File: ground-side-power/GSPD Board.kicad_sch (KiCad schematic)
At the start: 34 parts, among them J1 Battery Terminals, J2 Battery Terminals, J3 Battery Terminals, J4 Battery Terminals, J5 Battery Terminals, K1 AZ2150-1A-12DEF, SW1 23A, SW2 SW_SP3T, U1 K7805-3AR3, U2 URB2424LD-20WR3

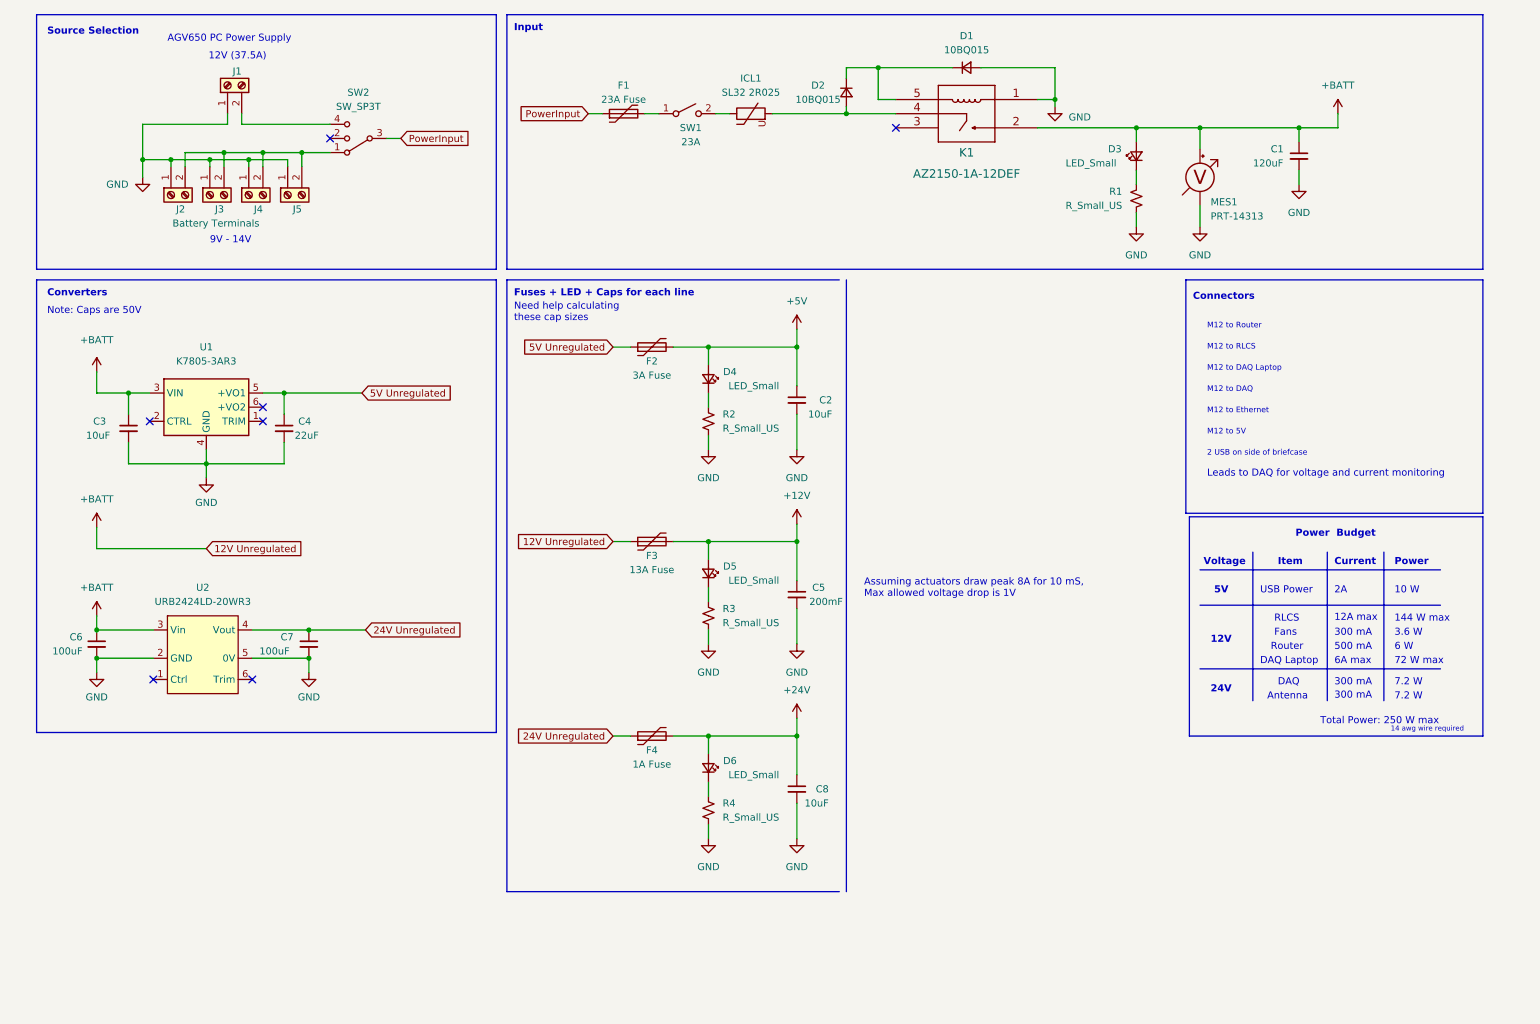
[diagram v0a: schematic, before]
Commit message: Added Screw Terminals for M12 connectors and switches
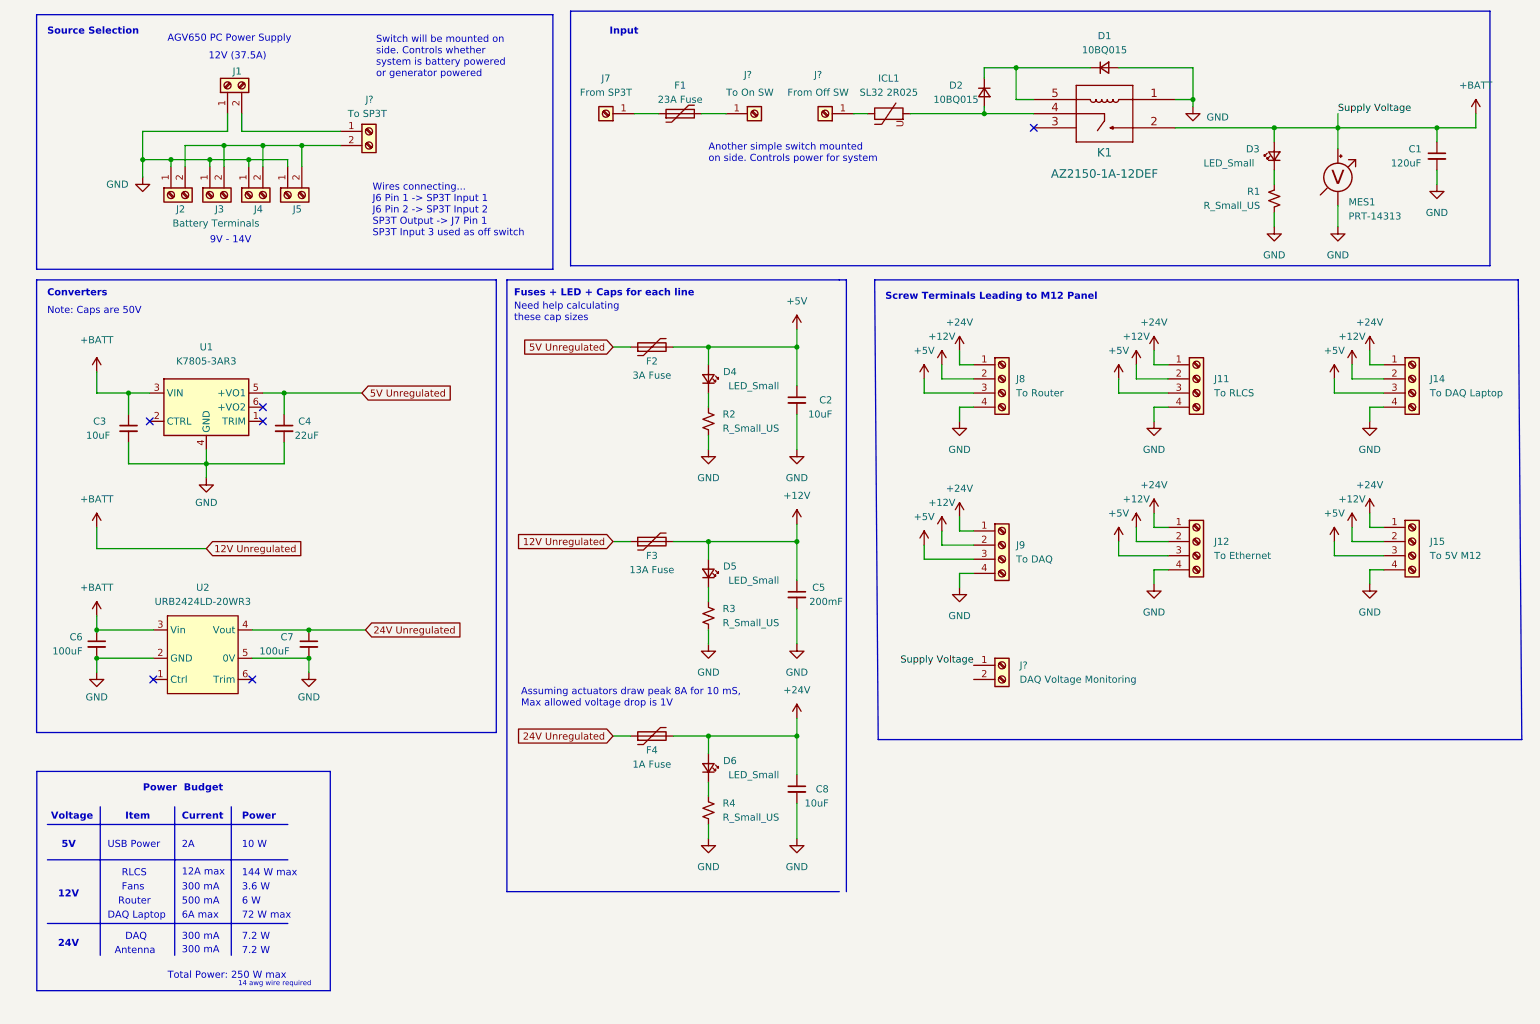
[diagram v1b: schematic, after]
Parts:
- removed SW1: 23A, symbol Switch:SW_SPST
- removed SW2: SW_SP3T, symbol Switch:SW_SP3T
- added J11: To RLCS, symbol Connector:Screw_Terminal_01x04
- added J12: To Ethernet, symbol Connector:Screw_Terminal_01x04
- added J14: To DAQ Laptop, symbol Connector:Screw_Terminal_01x04
- added J15: To 5V M12, symbol Connector:Screw_Terminal_01x04
- added J7: From SP3T, symbol Connector:Screw_Terminal_01x01
- added J8: To Router, symbol Connector:Screw_Terminal_01x04
- added J9: To DAQ, symbol Connector:Screw_Terminal_01x04
- added J?: To On SW, symbol Connector:Screw_Terminal_01x01
- added J?: From Off SW, symbol Connector:Screw_Terminal_01x01
- added J?: DAQ Voltage Monitoring, symbol Connector:Screw_Terminal_01x02
- added J?: To SP3T, symbol Connector:Screw_Terminal_01x02
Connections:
- net +12V: now also J11.2 (Pin_2), J12.2 (Pin_2), J14.2 (Pin_2), J15.2 (Pin_2), J8.2 (Pin_2), J9.2 (Pin_2)
- net +24V: now also J11.1 (Pin_1), J12.1 (Pin_1), J14.1 (Pin_1), J15.1 (Pin_1), J8.1 (Pin_1), J9.1 (Pin_1)
- net +5V: now also J11.3 (Pin_3), J12.3 (Pin_3), J14.3 (Pin_3), J15.3 (Pin_3), J8.3 (Pin_3), J9.3 (Pin_3)
- net +BATT: now also J?.1 (Pin_1)
- net GND: now also J11.4 (Pin_4), J12.4 (Pin_4), J14.4 (Pin_4), J15.4 (Pin_4), J8.4 (Pin_4), J9.4 (Pin_4)
- net at J2.2 (Pin_2), J3.2 (Pin_2), J4.2 (Pin_2)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: now also J?.2 (Pin_2)
- net at J1.2 (Pin_2): now also J?.1 (Pin_1)
- net at ICL1.1: now also J?.1 (Pin_1)
- net at F1.2: now also J?.1 (Pin_1)
- net PowerInput: no longer names the net of F1.1
- net PowerInput: now also J7.1 (Pin_1)
- no-connect marks 7 -> 6
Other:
- note added: "Another simple switch mounted on side. Controls power for system"
- note added: "Screw Terminals Leading to M12 Panel"
- note added: "Switch will be mounted on side. Controls whether system is battery powered or generator powered"
- note added: "Wires connecting... J6 Pin 1 -> SP3T Input 1 J6 Pin 2 -> SP3T Input 2 SP3T Output -> J7 Pin 1 SP3T Input 3 used as off switch"
- note removed: "2 USB on side of briefcase"
- note removed: "Connectors"
- note removed: "Leads to DAQ for voltage and current monitoring"
- note removed: "M12 to 5V"
- note removed: "M12 to DAQ"
- note removed: "M12 to DAQ Laptop"
- note removed: "M12 to Ethernet"
- note removed: "M12 to RLCS"
- note removed: "M12 to Router"
- moved on the sheet: C1, D1, D2, D3, F1, ICL1, K1, MES1, R1

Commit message: Added Current and Voltage Sensing for DAQ
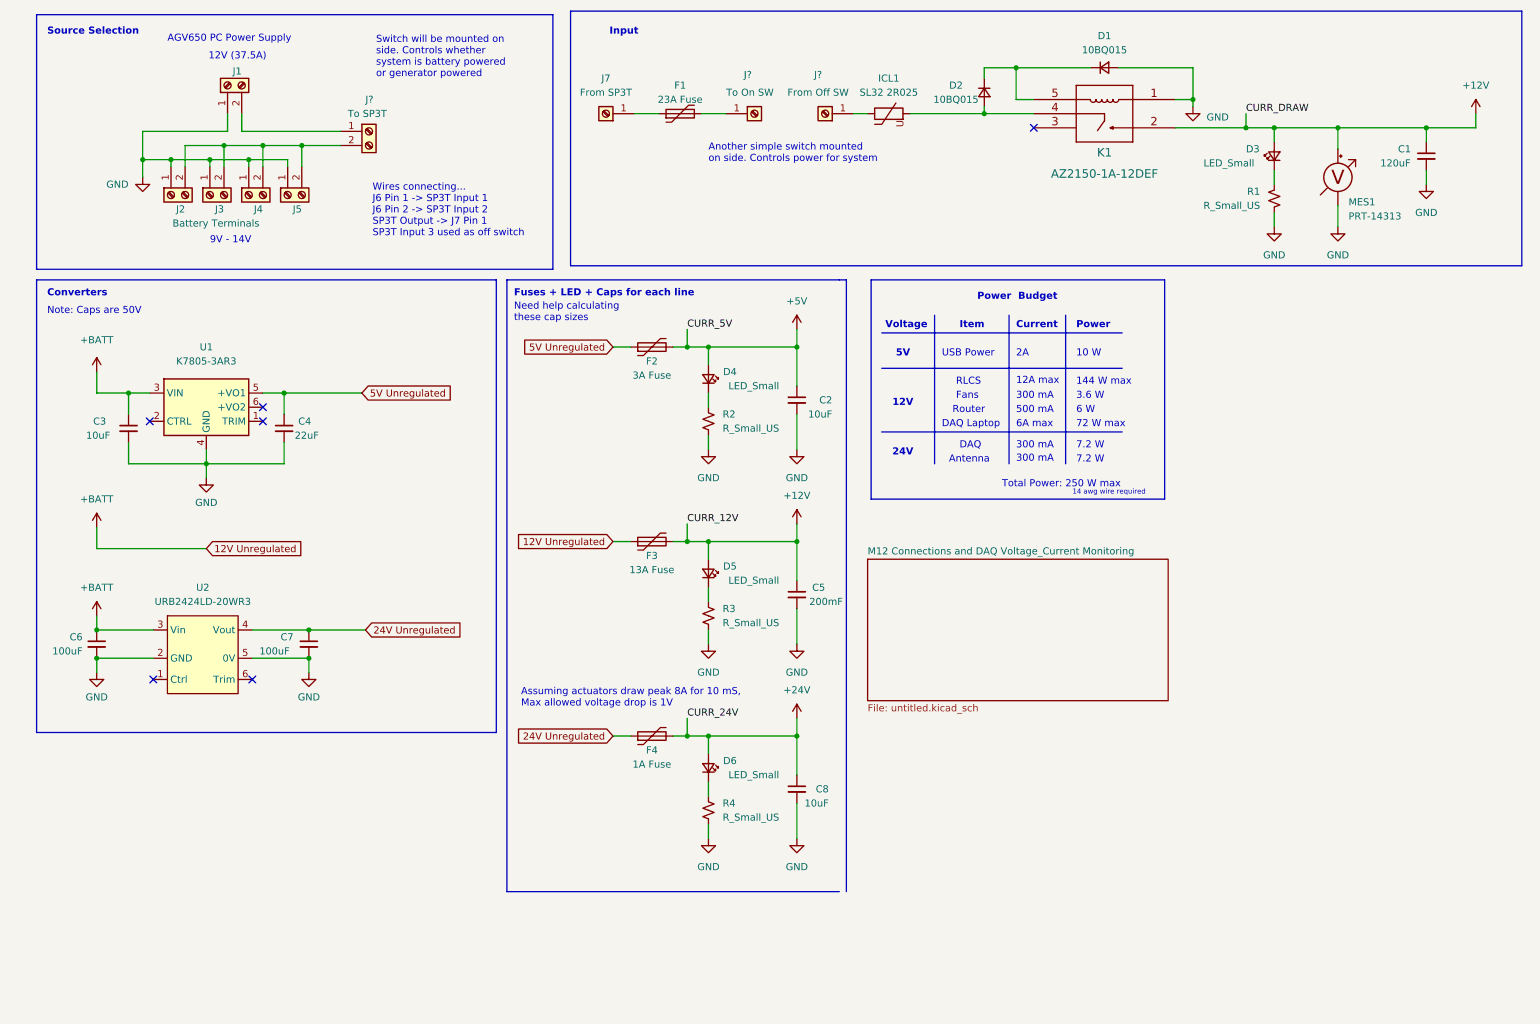
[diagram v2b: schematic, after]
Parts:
- removed J11: To RLCS, symbol Connector:Screw_Terminal_01x04
- removed J12: To Ethernet, symbol Connector:Screw_Terminal_01x04
- removed J14: To DAQ Laptop, symbol Connector:Screw_Terminal_01x04
- removed J15: To 5V M12, symbol Connector:Screw_Terminal_01x04
- removed J8: To Router, symbol Connector:Screw_Terminal_01x04
- removed J9: To DAQ, symbol Connector:Screw_Terminal_01x04
- removed J?: DAQ Voltage Monitoring, symbol Connector:Screw_Terminal_01x02
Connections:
- net +12V: now also C1.1, D3.2 (A), K1.2, MES1.2 (+)
- net +BATT: no longer C1.1, D3.2 (A), K1.2, MES1.2 (+)
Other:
- added sheet M12 Connections and DAQ Voltage_Current Monitoring (untitled.kicad_sch)
- note removed: "Screw Terminals Leading to M12 Panel"
- moved on the sheet: C1

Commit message: Addressed comments
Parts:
- removed C3: 10uF, symbol Device:C_Small
- removed C4: 22uF, symbol Device:C_Small
- added C?: 22uF, symbol Device:C_Small
- added C?: 10uF, symbol Device:C_Small
- J6: renamed from J?; value To SP3T -> To SP2T
- K1: footprint AZ2150_AMZ -> (none)
- U1: footprint Package_TO_SOT_SMD:TSOT-23-6 -> (none)
- gave numbers to parts that had none: 2
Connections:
- net +12V: no longer C1.1, D3.2 (A), K1.2, MES1.2 (+)
- net +BATT: now also C1.1, D3.2 (A), K1.2, MES1.2 (+), U1.2 (VIN), U1.4 (VIN), C?.1
- net GND: now also U1.5 (GND), U1.6 (GND), U1.7 (GND), U1.8 (GND), C?.2, C?.2; no longer U1.4 (GND)
- net 24V Unregulated: no longer names the net of C7.1, F4.1, U2.4 (Vout)
- net 5V Unregulated: no longer names the net of F2.1
- net 5V Unregulated: now also U1.9 (+VO1), C?.1; no longer U1.5 (+VO1)
- no-connect marks 6 -> 7
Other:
- sheet M12 Connections and DAQ Voltage_Current Monitoring ports: added 12V_UNSENSED, 24V_UNSENSED, 5V_UNSENSED, SYSTEM_UNSENSED; removed none
- note added: "Assuming actuators draw peak 8A for 10 mS, max allowed voltage drop is 1V"
- note added: "Wires connecting... J6 Pin 1 -> SP3T Input 1 J6 Pin 2 -> SP3T Input 2 SP3T Output -> J7 Pin 1"
- note removed: "Assuming actuators draw peak 8A for 10 mS, Max allowed voltage drop is 1V"
- note removed: "Wires connecting... J6 Pin 1 -> SP3T Input 1 J6 Pin 2 -> SP3T Input 2 SP3T Output -> J7 Pin 1 SP3T Input 3 used as off switch"
- moved on the sheet: C2, C5, C6, C7, C8, D4, D5, D6, F2, F3, F4, R2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

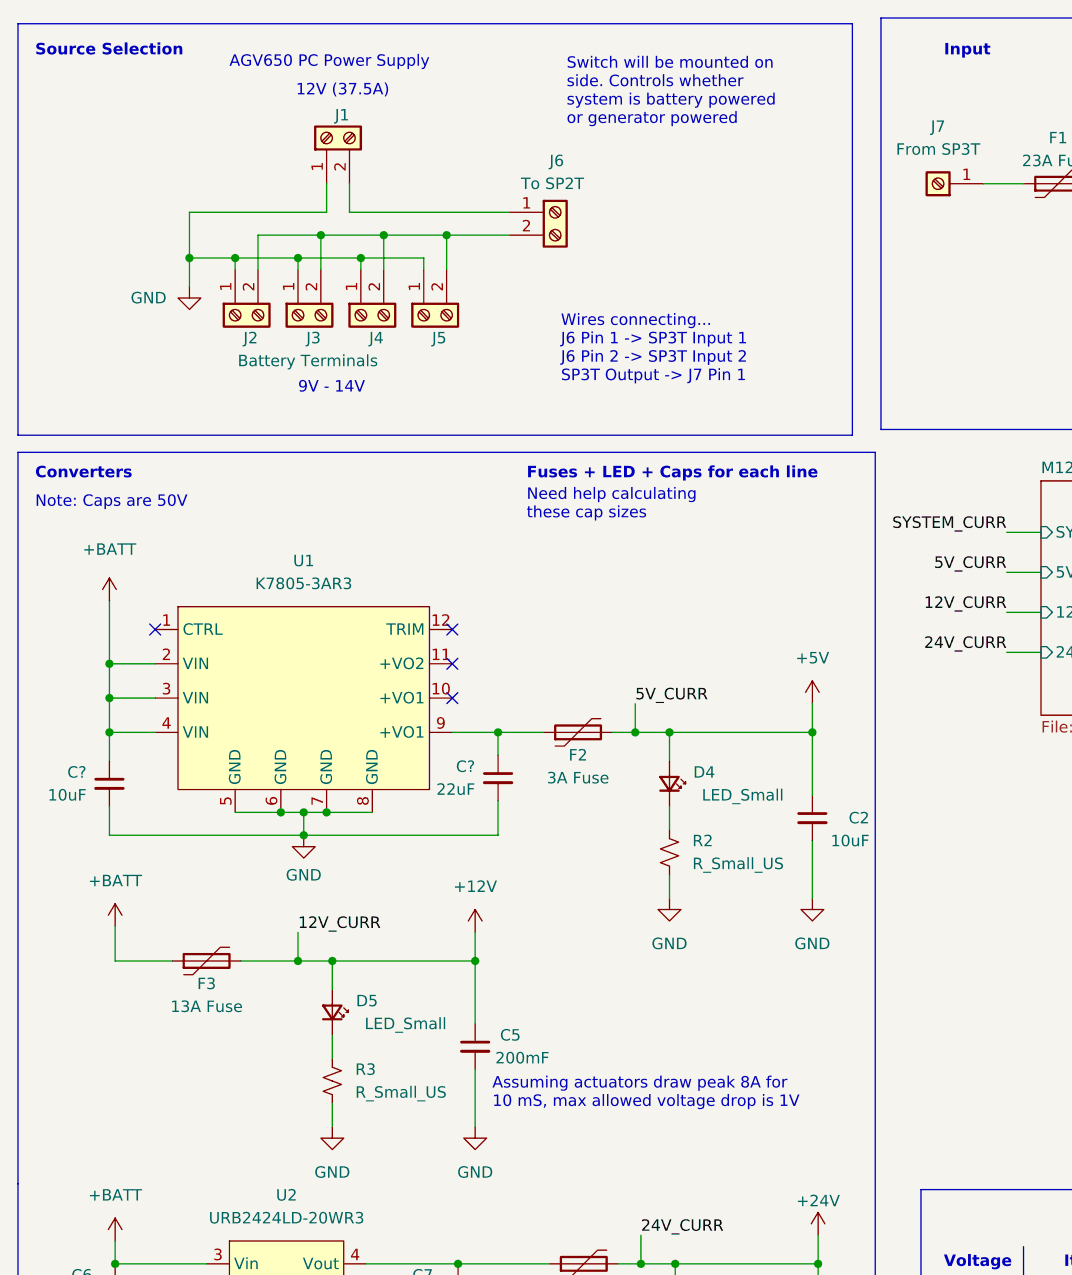
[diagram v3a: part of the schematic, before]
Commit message: Added correct PSU connector
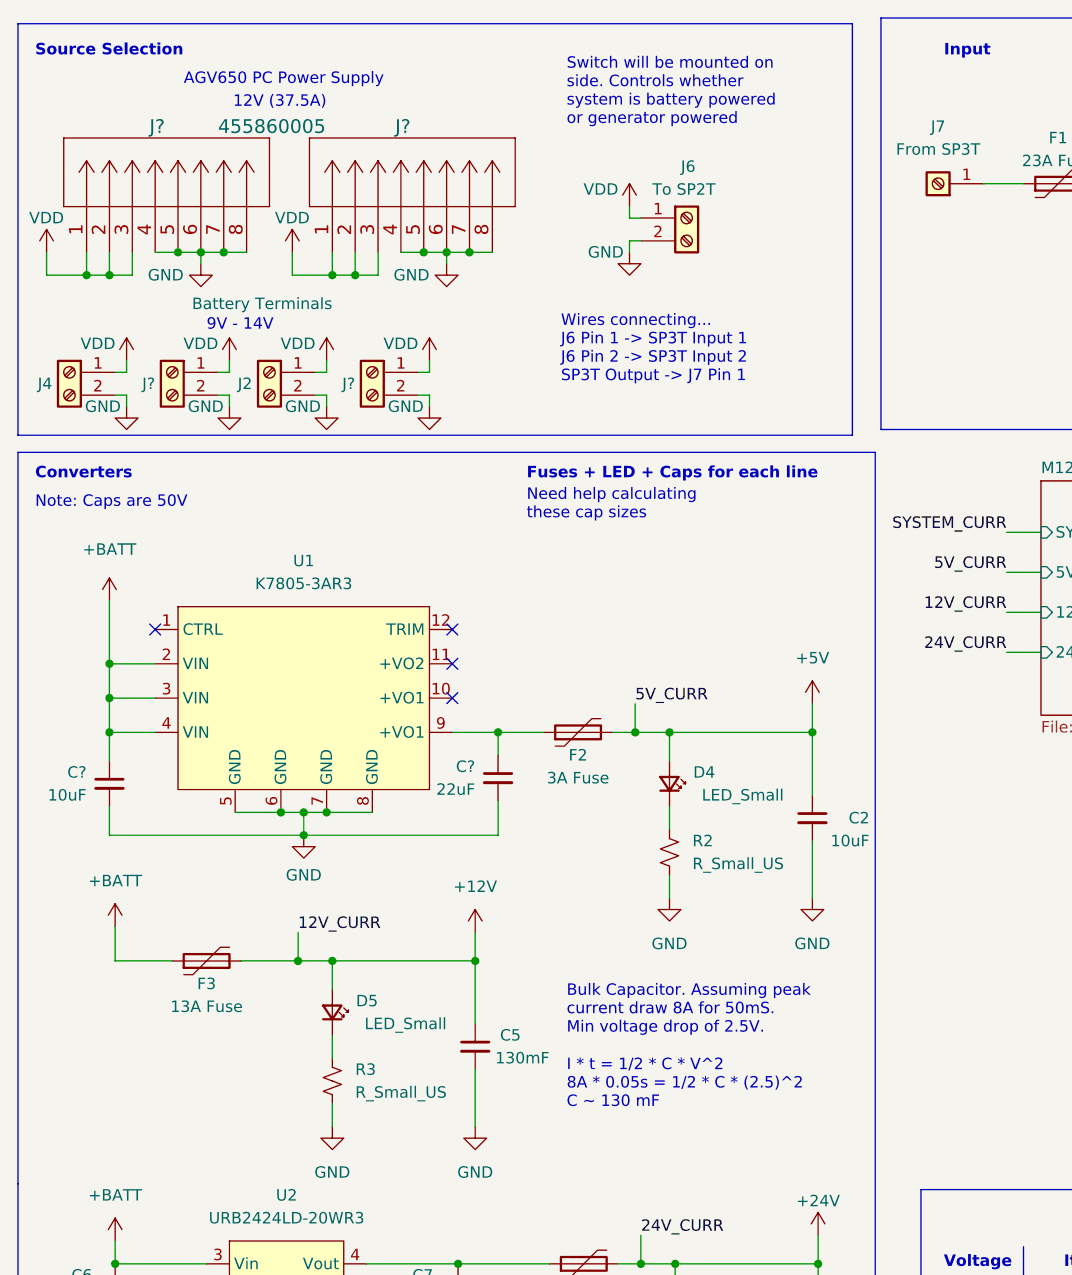
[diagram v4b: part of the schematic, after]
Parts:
- removed J1, J3, J5: Battery Terminals, symbol Connector:Screw_Terminal_01x02
- added J? (x2): 455860005, CON_455860005_MOL, symbol GSP:455860005
- added J? (x2): Battery Terminals, symbol Connector:Screw_Terminal_01x02
- C5: value 200mF -> 130mF
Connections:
- net GND: now also J2.2 (Pin_2), J4.2 (Pin_2), J6.2 (Pin_2), J?.2 (Pin_2), J?.2 (Pin_2), J?.4, J?.4, J?.5, J?.5, J?.6, J?.6, J?.7, J?.7, J?.8, J?.8; no longer J2.1 (Pin_1), J4.1 (Pin_1)
- net VDD: now reaches J6.1 (Pin_1)
- net VDD: now also J2.1 (Pin_1), J4.1 (Pin_1), J?.1, J?.1, J?.1 (Pin_1), J?.1 (Pin_1), J?.2, J?.2, J?.3, J?.3
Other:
- note added: "Bulk Capacitor. Assuming peak current draw 8A for 50mS. Min voltage drop of 2.5V."
- note added: "I * t = 1/2 * C * V^2 8A * 0.05s = 1/2 * C * (2.5)^2 C ~ 130 mF"
- note removed: "Assuming actuators draw peak 8A for 10 mS, max allowed voltage drop is 1V"
- moved on the sheet: J2, J4, J6
